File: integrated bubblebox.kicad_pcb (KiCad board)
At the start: 2 copper layers, 291.3 x 133.4 mm, 63 parts, among them J1 USB C Connector, J2 JTAG_TC2030, M1 SW_Push, M2 SW_Push, SW1 Boot, U1 XC6206, U2 USBLC6-2SC6, U3 RP2040, U4 W25Q128JVS, X1 SW_Push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

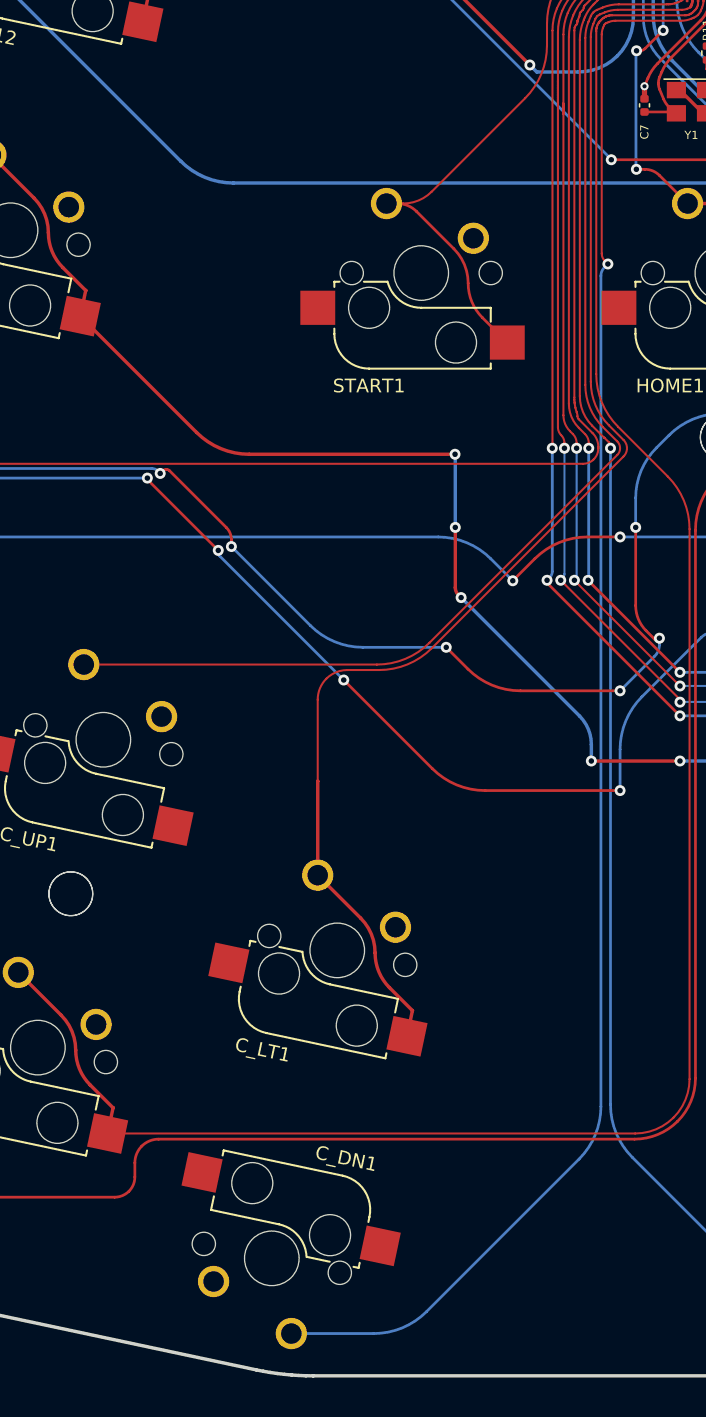
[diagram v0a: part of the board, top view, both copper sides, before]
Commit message: Fixed hotswap connection on C-Up and C-Down, and also fixed RP2040 Gnd.
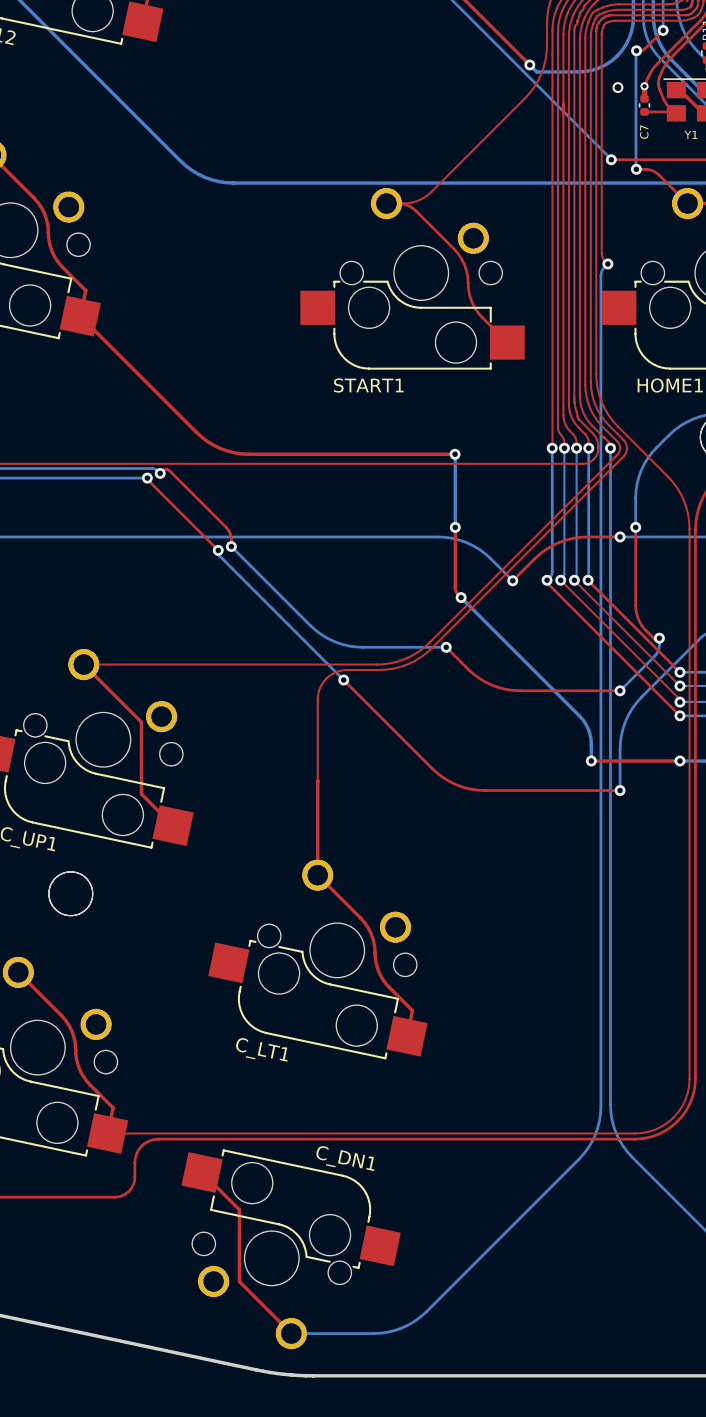
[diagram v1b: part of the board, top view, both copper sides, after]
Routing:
- net C_UP: track 85.5 -> 100.0 mm
- net C_DN: track 118.2 -> 132.6 mm
- net GND: track 49.5 -> 49.6 mm, vias 18 -> 19
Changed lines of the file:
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@@
 		)
 		(pad "2" smd rect
-			(at 7.56 -2.540001 168)
+			(at 7.56 -2.540002 168)
 			(size 2.55 2.5)
 			(layers "F.Cu" "F.Paste" "F.Mask")
@@
 		)
 		(pad "2" smd rect
-			(at 7.56 -2.540001 168)
+			(at 7.56 -2.540002 168)
 			(size 2.55 2.5)
 			(layers "F.Cu" "F.Paste" "F.Mask")
@@
 		)
 		(pad "2" smd rect
-			(at 7.56 -2.540001 348)
+			(at 7.56 -2.540002 348)
 			(size 2.55 2.5)
 			(layers "F.Cu" "F.Paste" "F.Mask")
@@
 		)
 		(pad "2" smd rect
-			(at 7.56 -2.540001 168)
+			(at 7.56 -2.540002 168)
 			(size 2.55 2.5)
 			(layers "F.Cu" "F.Paste" "F.Mask")
@@
 		)
 		(pad "2" smd rect
-			(at 7.56 -2.540001 168)
+			(at 7.56 -2.540002 168)
 			(size 2.55 2.5)
 			(layers "F.Cu" "F.Paste" "F.Mask")
@@
 		)
 		(pad "2" smd rect
-			(at 7.56 -2.540001 168)
+			(at 7.56 -2.540002 168)
 			(size 2.55 2.5)
 			(layers "F.Cu" "F.Paste" "F.Mask")
@@
 		)
 		(pad "2" smd rect
-			(at 7.56 -2.540001 168)
+			(at 7.56 -2.540002 168)
 			(size 2.55 2.5)
 			(layers "F.Cu" "F.Paste" "F.Mask")
@@
 		)
 		(pad "2" smd rect
-			(at 7.56 -2.540001 168)
+			(at 7.56 -2.540002 168)
 			(size 2.55 2.5)
 			(layers "F.Cu" "F.Paste" "F.Mask")
@@
 		)
 		(pad "2" smd rect
-			(at 7.56 -2.540001 168)
+			(at 7.56 -2.540002 168)
 			(size 2.55 2.5)
 			(layers "F.Cu" "F.Paste" "F.Mask")
@@
 		)
 		(pad "2" smd rect
-			(at 7.56 -2.540001 168)
+			(at 7.56 -2.540002 168)
 			(size 2.55 2.5)
 			(layers "F.Cu" "F.Paste" "F.Mask")
@@
 		)
 		(pad "2" smd rect
-			(at 7.56 -2.540001 168)
+			(at 7.56 -2.540002 168)
 			(size 2.55 2.5)
 			(layers "F.Cu" "F.Paste" "F.Mask")
@@
 		)
 		(pad "2" smd rect
-			(at 7.56 -2.540001 168)
+			(at 7.56 -2.540002 168)
 			(size 2.55 2.5)
 			(layers "F.Cu" "F.Paste" "F.Mask")
@@
 		)
 		(pad "2" smd rect
-			(at 7.56 -2.540001 168)
+			(at 7.56 -2.540002 168)
 			(size 2.55 2.5)
 			(layers "F.Cu" "F.Paste" "F.Mask")
@@
 	)
 	(via
+		(at 192.38 72.45)
+		(size 0.8)
+		(drill 0.5)
+		(layers "F.Cu" "B.Cu")
+		(net 1)
+	)
+	(via
 		(at 206.992 56.513)
 		(size 0.6)
@@
 	)
 	(segment
+		(start 192.32 72.54)
+		(end 192.38 72.48)
+		(width 0.25)
+		(layer "B.Cu")
+		(net 1)
+	)
+	(segment
 		(start 201.31 61.063)
 		(end 200.0356 61.063)
@@
 	)
 	(segment
+		(start 192.38 72.48)
+		(end 192.38 72.45)
+		(width 0.25)
+		(layer "B.Cu")
+		(net 1)
+	)
+	(segment
 		(start 198.76 62.3379)
 		(end 198.76 61.0631)
@@
 	)
 	(segment
+		(start 164.7142 159.711582)
+		(end 164.7142 154.462403)
+		(width 0.25)
+		(layer "F.Cu")
+		(net 49)
+	)
+	(segment
 		(start 191.524195 67.736967)
 		(end 191.7035 67.66275)
@@
 	)
 	(segment
+		(start 164.7142 154.462403)
+		(end 161.986743 151.734946)
+		(width 0.25)
+		(layer "F.Cu")
+		(net 49)
+	)
+	(segment
 		(start 191.194 84.577102)
 		(end 191.194 68.561516)
@@
 	)
 	(segment
+		(start 168.511404 163.508786)
+		(end 164.7142 159.711582)
+		(width 0.25)
+		(layer "F.Cu")
+		(net 49)
+	)
+	(segment
 		(start 191.643 85.344)
 		(end 191.4185 85.11935)
@@
 	)
 	(segment
+		(start 159.867957 126.390354)
+		(end 157.558438 124.080835)
+		(width 0.25)
+		(layer "F.Cu")
+		(net 51)
+	)
+	(segment
 		(start 197.015487 66.095044)
 		(end 197.016655 66.094371)
@@
 		(layer "F.Cu")
 		(net 51)
+	)
+	(segment
+		(start 157.558438 118.831656)
+		(end 153.343296 114.616514)
+		(width 0.25)
+		(layer "F.Cu")
+		(net 51)
+	)
+	(segment
+		(start 157.558438 124.080835)
+		(end 157.558438 118.831656)
+		(width 0.25)
+		(layer "F.Cu")
+		(net 51)
